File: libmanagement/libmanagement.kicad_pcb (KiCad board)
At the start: 2 copper layers, 2 parts

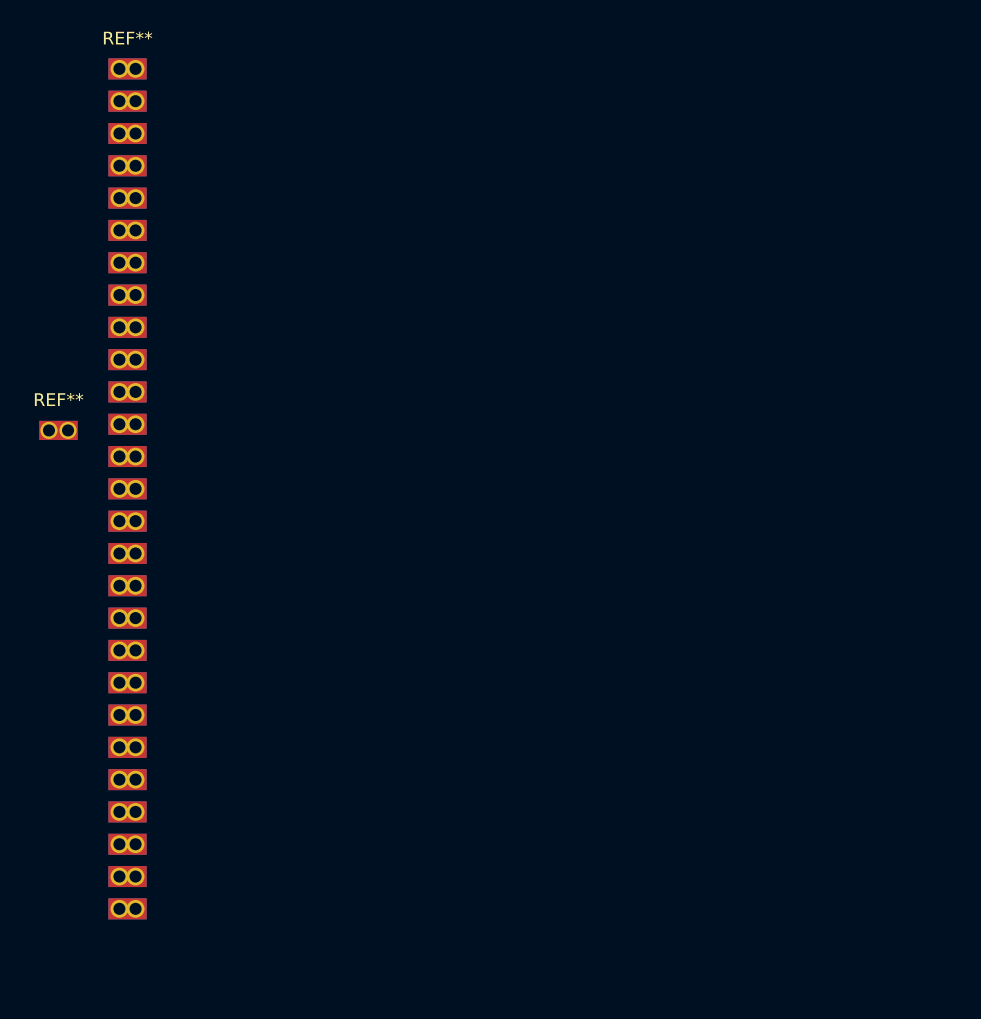
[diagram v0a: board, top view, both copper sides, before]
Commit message: A few extra antennas
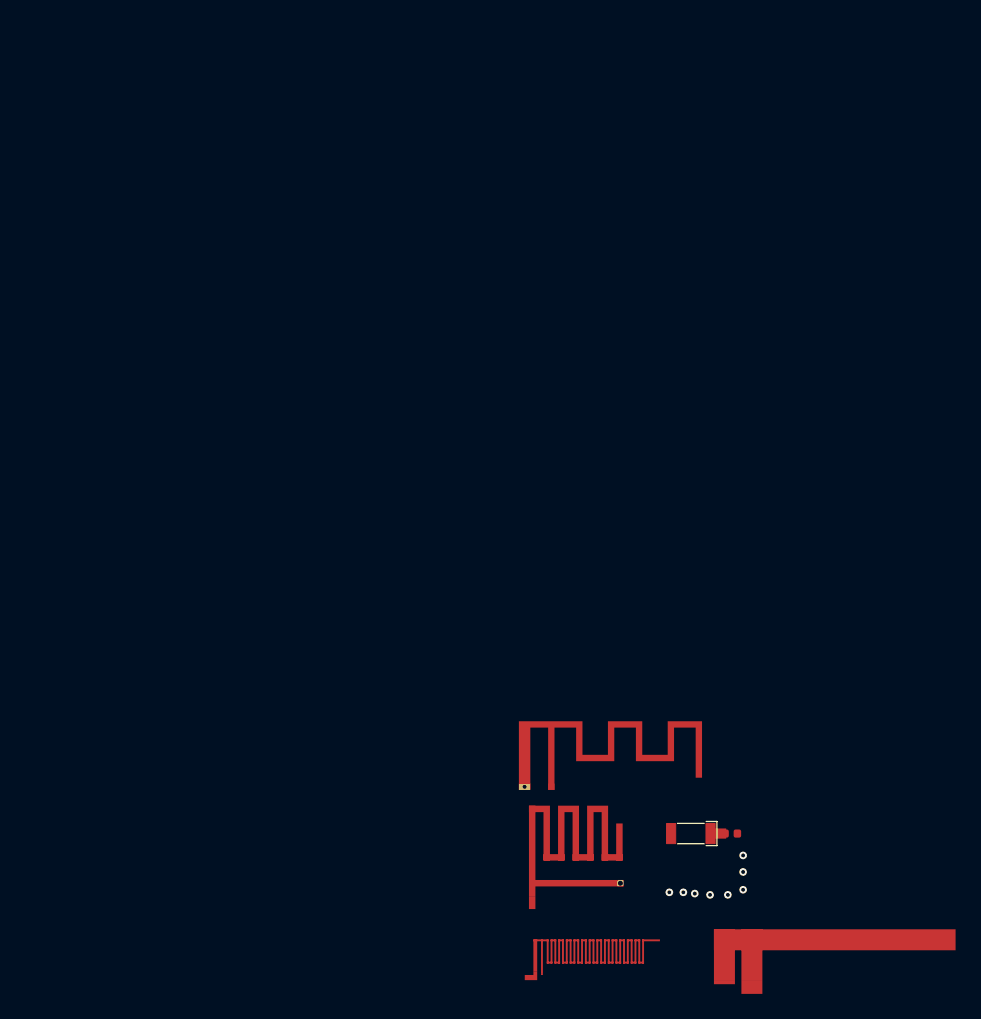
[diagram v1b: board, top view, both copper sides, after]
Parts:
- removed the REF** at (107.5, 73.2)
- removed the REF** at (112.9, 44.8)
- added AE1: Antenna_Chip, PCM_ckl-misc:Walsin_RFANT3216120A5T, F.Cu at (157.2, 104.9)
- added L1: 6.8nH, Inductor_SMD:L_0402_1005Metric, F.Cu at (160.4, 104.9)
- added REF**: Texas_SWRA117D_2.4GHz_Right, RF_Antenna:Texas_SWRA117D_2.4GHz_Right, F.Cu at (146.2, 101.2)
- added REF**: WCH_CH572_2.4GHz, WIP_ckl-misc:ANT_WCH_2.4GHz_1, F.Cu at (149.6, 116.0)
- added REF**: ANT_CYPRESS_MIFA_1.6mm, WIP_ckl-misc:ANT_CYPRESS_MIFA_1.6mm, F.Cu at (145.0, 109.8)
- added REF**: ANT_CYPRESS_IFA_1.6mm, WIP_ckl-misc:ANT_CYPRESS_IFA_1.6mm, F.Cu at (162.0, 116.5)
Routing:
- net (no net): vias 0 -> 8
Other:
- copper layers 2 -> 4
